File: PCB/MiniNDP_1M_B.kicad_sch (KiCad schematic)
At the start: 18 parts, among them J1 Conn_02x20_Odd_Even, U1 HC161, U2 HC161, U3 HC161, U4 HC138, U5 FCT821, U6 AS6C4008, U7 1G32

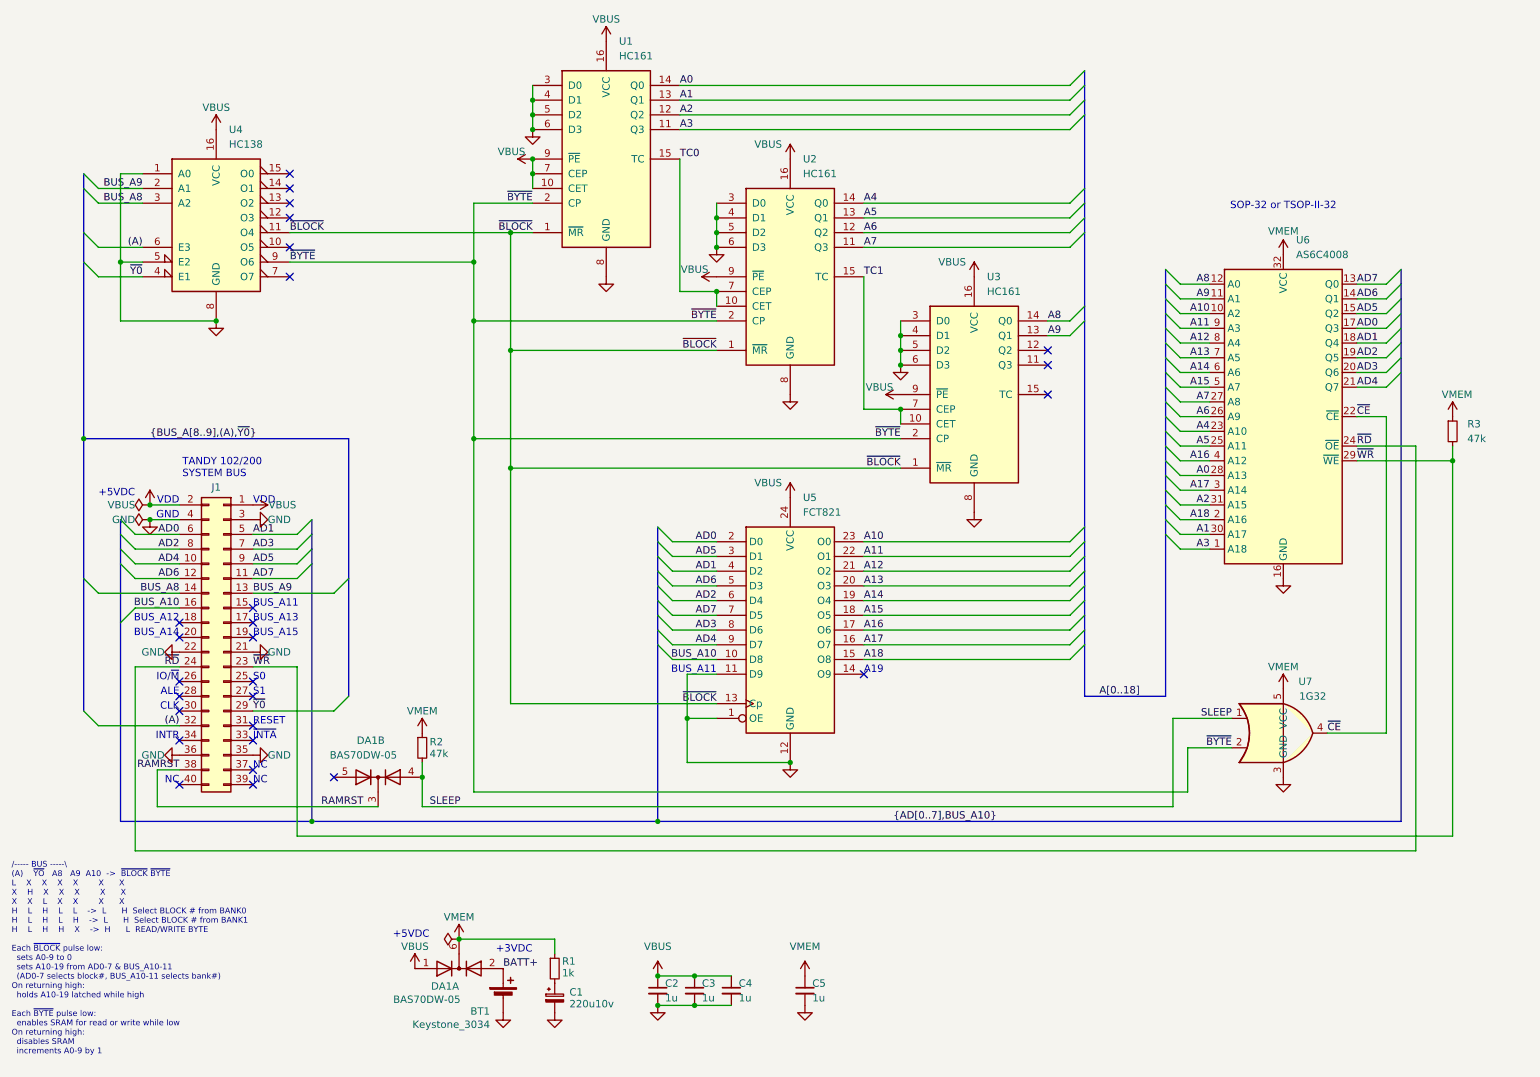
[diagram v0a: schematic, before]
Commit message: add 1M_B version
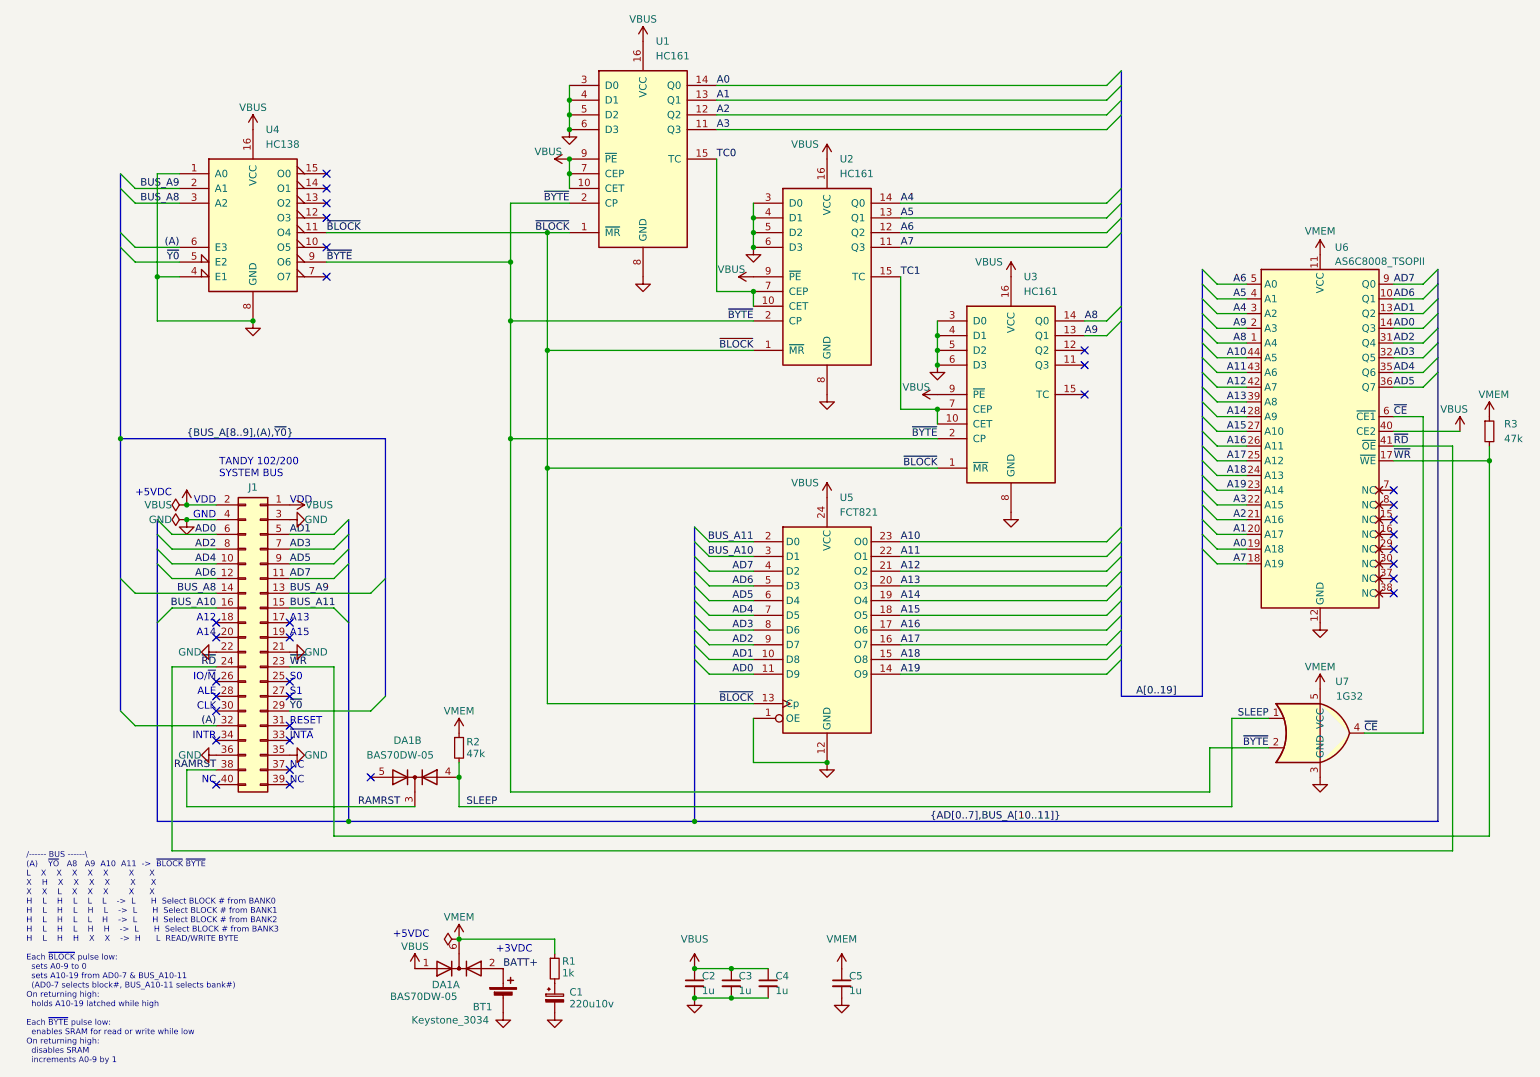
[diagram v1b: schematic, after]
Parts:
- removed U6: AS6C4008, 000_LOCAL:TSOP-II-SOP-32_dual, symbol 000_LOCAL:AS6C4008_DIP
- added U6: AS6C8008_TSOPII, 000_LOCAL:TSOP-II-44, symbol 000_LOCAL:AS6C8008_TSOPII
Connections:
- net A0: now also U6.19 (A18)
- net A1: now also U6.20 (A17)
- net A10: now also U6.44 (A5)
- net A11: now also U6.43 (A6)
- net A12: now also U6.42 (A7)
- net A13: now also U6.39 (A8)
- net A14: now also U6.28 (A9)
- net A15: now also U6.27 (A10)
- net A16: now also U6.26 (A11)
- net A17: now also U6.25 (A12)
- net A18: now also U6.24 (A13)
- net A2: now also U6.21 (A16)
- net A3: now also U6.22 (A15)
- net A4: now also U6.3 (A2)
- net A5: now also U6.4 (A1)
- net A6: now also U6.5 (A0)
- net A7: now also U6.18 (A19)
- net A8: now also U6.1 (A4)
- net A9: now also U6.2 (A3)
- net AD0: now also U5.11 (D9), U6.14 (Q3); no longer U5.2 (D0)
- net AD1: now also U5.10 (D8), U6.13 (Q2); no longer U5.4 (D2)
- net AD2: now also U5.9 (D7), U6.31 (Q4); no longer U5.6 (D4)
- net AD3: now also U6.32 (Q5)
- net AD4: now also U5.7 (D5), U6.35 (Q6); no longer U5.9 (D7)
- net AD5: now also U5.6 (D4), U6.36 (Q7); no longer U5.3 (D1)
- net AD6: now also U6.10 (Q1)
- net AD7: now also U5.4 (D2), U6.9 (Q0); no longer U5.7 (D5)
- net BUS_A10: now also U5.3 (D1); no longer U5.10 (D8)
- net GND: now also U4.4 (E1), U6.12 (GND), U6.34 (GND); no longer U4.5 (E2), U5.11 (D9)
- net VBUS: now also U6.40 (CE2)
- net VMEM: now also U6.11 (VCC), U6.33 (VCC)
- net ~{CE}: now also U6.6 (~{CE1})
- net ~{RD}: now also U6.41 (~{OE})
- net ~{WR}: now also U6.17 (~{WE})
- net ~{Y0}: now also U4.5 (E2); no longer U4.4 (E1)
- net A19: now reaches U5.14 (O9)
- net A19: now also U6.23 (A14)
- net BUS_A11: now reaches J1.15 (Pin_15)
- net BUS_A11: now also U5.2 (D0)
- no-connect marks 27 -> 33
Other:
- note added: "/------ BUS ------\ (A) ~{YO} A8 A9 A10 A11 -> ~{BLOCK} ~{BYTE} L X X X X X X X X H X X X X X X X X L X X X X X H L H L L L -> L H Select BLOCK # from BANK0 H L H L H L -> L H Select BLOCK # from BANK1 H L H L L H -> L H Select BLOCK # from BANK2 H L H L H H -> L H Select BLOCK # from BANK3 H L H H X X -> H L READ/WRITE BYTE Each ~{BLOCK} pulse low: sets A0-9 to 0 sets A10-19 from AD0-7 & BUS_A10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"
- note added: "A12"
- note added: "A13"
- note added: "A14"
- note added: "A15"
- note removed: "/----- BUS -----\ (A) ~{YO} A8 A9 A10 -> ~{BLOCK} ~{BYTE} L X X X X X X X H X X X X X X X L X X X X H L H L L -> L H Select BLOCK # from BANK0 H L H L H -> L H Select BLOCK # from BANK1 H L H H X -> H L READ/WRITE BYTE Each ~{BLOCK} pulse low: sets A0-9 to 0 sets A10-19 from AD0-7 & BUS_A10-11 (AD0-7 selects block#, BUS_A10-11 selects bank#) On returning high: holds A10-19 latched while high Each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"
- note removed: "A19"
- note removed: "BUS_A11"
- note removed: "BUS_A12"
- note removed: "BUS_A13"
- note removed: "BUS_A14"
- note removed: "BUS_A15"
- note removed: "SOP-32 or TSOP-II-32"
- title: MiniNDP 512K -> MiniNDP 1M
- moved on the sheet: C2, C3, C4, DA1B, J1, R2, R3, U1, U2, U3, U4, U5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

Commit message: 1M_B & 512_B
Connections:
- net BATT+ renamed +BATT
- net ~{CE} renamed ~{CE1}
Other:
- note added: "3V"
- note added: "5V"
- note added: "CR2032"
- note removed: "+3VDC"
- moved on the sheet: BT1, C1, DA1A, DA1B, R1, R2, U1, U2, U3, U5
